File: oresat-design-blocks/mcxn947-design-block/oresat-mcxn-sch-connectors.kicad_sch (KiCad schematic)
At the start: 16 parts, among them J10 Conn_02x20_Odd_Even, J2 USB_C_Receptacle_USB2.0_14P, J9 Conn_02x20_Odd_Even, U1 MCXN947VKLT

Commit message: Updated BOM with MPNs and fixed one missing 0805 footprint error, rev'd board to v1.1
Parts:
- C1: MFR (none) -> Murata Electronics; MPN (none) -> GRM188R72A104KA35D
- J10, J9: MFR (none) -> Adam Tech; MPN (none) -> PH2-20-UA
- J2: MFR (none) -> GCT; MPN (none) -> USB4105-GF-A
- J7: value ~ -> OreSat Debug; MFR (none) -> TE; MPN (none) -> 2-1734592-0
- R1, R2: MFR (none) -> Stackpole Electronics Inc; MPN (none) -> RMCF0603FT5K11
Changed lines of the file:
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@@
 			)
 		)
-		(property "Description" "Resistor, small US symbol"
+		(property "Description" "5.11 kOhms ±1% 0.1W, 1/10W Chip Resistor 0603 (1608 Metric) Automotive AEC-Q200 Thick Film"
+			(at 306.07 90.17 0)
+			(effects
+				(font
+					(size 1.27 1.27)
+				)
+				(hide yes)
+			)
+		)
+		(property "MFR" "Stackpole Electronics Inc"
+			(at 306.07 90.17 0)
+			(effects
+				(font
+					(size 1.27 1.27)
+				)
+				(hide yes)
+			)
+		)
+		(property "MPN" "RMCF0603FT5K11"
 			(at 306.07 90.17 0)
 			(effects
@@
 			)
 		)
+		(property "MFR" "Adam Tech"
+			(at 100.33 177.8 0)
+			(effects
+				(font
+					(size 1.27 1.27)
+				)
+				(hide yes)
+			)
+		)
+		(property "MPN" "PH2-20-UA"
+			(at 100.33 177.8 0)
+			(effects
+				(font
+					(size 1.27 1.27)
+				)
+				(hide yes)
+			)
+		)
 		(pin "35"
 		)
@@
 			)
 		)
-		(property "Value" "~"
+		(property "Value" "OreSat Debug"
 			(at 367.03 71.12 0)
 			(effects
@@
 			)
 		)
-		(property "Datasheet" ""
+		(property "Datasheet" "https://www.te.com/usa-en/product-2-1734592-0.datasheet.pdf"
+			(at 367.03 71.12 0)
+			(effects
+				(font
+					(size 1.27 1.27)
+				)
+				(hide yes)
+			)
+		)
+		(property "Description" "20 Position FPC Connector Contacts, Bottom 0.020\" (0.50mm) Surface Mount, Right Angle"
+			(at 367.03 71.12 0)
+			(effects
+				(font
+					(size 1.27 1.27)
+				)
+				(hide yes)
+			)
+		)
+		(property "MFR" "TE"
 			(at 367.03 71.12 0)
 			(effects
@@
 			)
 		)
-		(property "Description" ""
+		(property "MPN" "2-1734592-0"
 			(at 367.03 71.12 0)
 			(effects
@@
 			)
 		)
-		(property "Description" "Resistor, small US symbol"
+		(property "Description" "5.11 kOhms ±1% 0.1W, 1/10W Chip Resistor 0603 (1608 Metric) Automotive AEC-Q200 Thick Film"
+			(at 312.42 90.17 0)
+			(effects
+				(font
+					(size 1.27 1.27)
+				)
+				(hide yes)
+			)
+		)
+		(property "MFR" "Stackpole Electronics Inc"
+			(at 312.42 90.17 0)
+			(effects
+				(font
+					(size 1.27 1.27)
+				)
+				(hide yes)
+			)
+		)
+		(property "MPN" "RMCF0603FT5K11"
 			(at 312.42 90.17 0)
 			(effects
@@
 			)
 		)
+		(property "MFR" "Adam Tech"
+			(at 110.49 82.55 0)
+			(effects
+				(font
+					(size 1.27 1.27)
+				)
+				(hide yes)
+			)
+		)
+		(property "MPN" "PH2-20-UA"
+			(at 110.49 82.55 0)
+			(effects
+				(font
+					(size 1.27 1.27)
+				)
+				(hide yes)
+			)
+		)
 		(pin "35"
 		)
@@
 			)
 		)
-		(property "Datasheet" "~"
+		(property "Datasheet" "https://search.murata.co.jp/Ceramy/image/img/A01X/G101/ENG/GRM188R72A104KA35-01.pdf"
 			(at 275.59 91.44 0)
 			(effects
@@
 			)
 		)
-		(property "Description" "Unpolarized capacitor, small symbol"
+		(property "Description" "0.1 µF ±10% 100V Ceramic Capacitor X7R 0603 (1608 Metric)"
+			(at 275.59 91.44 0)
+			(effects
+				(font
+					(size 1.27 1.27)
+				)
+				(hide yes)
+			)
+		)
+		(property "MFR" "Murata Electronics"
+			(at 275.59 91.44 0)
+			(effects
+				(font
+					(size 1.27 1.27)
+				)
+				(hide yes)
+			)
+		)
+		(property "MPN" "GRM188R72A104KA35D"
 			(at 275.59 91.44 0)
 			(effects
@@
 			)
 		)
-		(property "Datasheet" "https://www.usb.org/sites/default/files/documents/usb_type-c.zip"
+		(property "Datasheet" "https://gct.co/files/specs/usb4105-spec.pdf"
 			(at 287.02 63.5 0)
 			(effects
@@
 			)
 		)
-		(property "Description" "USB 2.0-only 14P Type-C Receptacle connector"
+		(property "Description" "USB-C (USB TYPE-C) USB 2.0 Receptacle Connector 24 (16+8 Dummy) Position Surface Mount, Right Angle; Through Hole"
+			(at 283.21 63.5 0)
+			(effects
+				(font
+					(size 1.27 1.27)
+				)
+				(hide yes)
+			)
+		)
+		(property "MFR" "GCT"
+			(at 283.21 63.5 0)
+			(effects
+				(font
+					(size 1.27 1.27)
+				)
+				(hide yes)
+			)
+		)
+		(property "MPN" "USB4105-GF-A"
 			(at 283.21 63.5 0)
 			(effects

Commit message: Cleanup of page names and put all power/connectors and signals on the same page facing the same way
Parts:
- removed J10, J9: Conn_02x20_Odd_Even, Connector_PinHeader_2.54mm:PinHeader_2x20_P2.54mm_Vertical, symbol Connector_Generic:Conn_02x20_Odd_Even
- removed U1: MCXN947VKLT, oresat-ics:MCXN947KVLT-QFP50P1600X1600X160-101N, symbol oresat-ics:MCXN947VKLT
- added C10: 6.8u, oresat-passives:0603-C-NOSILK, symbol Device:C_Small
- added C11, C7: 4.7u, oresat-passives:0603-C-NOSILK, symbol Device:C_Small
- added C12, C13, C14, C15, C16, C2, C20, C3, C8, C9: 100n, oresat-passives:0603-C-NOSILK, symbol Device:C_Small
- added C17, C4: 1u, oresat-passives:0603-C-NOSILK, symbol Device:C_Small
- added C18: 22u, oresat-passives:0805-C-NOSILK, symbol Device:C
- added C5: 10u, oresat-passives:0603-C-NOSILK, symbol Device:C
- added C6: 2.2u, oresat-passives:0603-C-NOSILK, symbol Device:C_Small
- added D1: BAT54CW, Package_TO_SOT_SMD:SOT-323_SC-70, symbol Diode:BAT54CW
- added D6: GREEN, LED_SMD:LED_0603_1608Metric, symbol Device:LED_Small_Filled
- added FB1: 120 ohm, oresat-passives:0805-B-NOSILK, symbol Device:FerriteBead_Small
- added J1: BKUP-BATT, Connector_PinHeader_2.54mm:PinHeader_1x02_P2.54mm_Vertical, symbol Connector_Generic:Conn_01x02
- added L1: 1.5u, Inductor_SMD:L_0805_2012Metric, symbol Device:L_Small
- added L2: 6.8u, oresat-passives:L_ECS-MPI4040, symbol oresat-passives:L_BIG
- added R10, R11, R12: 10k, oresat-passives:0603-C-NOSILK, symbol oresat-passives:R-US
- added R3: 10k, oresat-passives:0603-C-NOSILK, symbol Device:R_Small_US
- added TP1, TP2, TP3, TP33, TP34, TP4: Test-Point, oresat-misc:TestPoint-0.75mm-th, symbol oresat-misc:Test-Point-0.75mm-th
- added U1: MCXN947VKLT, oresat-ics:MCXN947KVLT-QFP50P1600X1600X160-101N, symbol oresat-ics:MCXN947VKLT
- added U3: TPS62111RSA, Package_DFN_QFN:Texas_RSA_VQFN-16-1EP_4x4mm_P0.65mm_EP2.7x2.7mm, symbol oresat-ics:TPS6211X
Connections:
- net +3.3V: now also C12.1, C13.1, C14.1, C15.1, C16.1, C18.1, C7.1, C8.1, C9.1, D1.2, FB1.1, L2.2, R10.2, R3.2, TP34.1, U1.34 (VDD_P4), U1.44 (VDD_USB), U1.54 (VDD_DCDC/VDD_LDO_SYS), U1.59 (VDD_P3_1), U1.66 (VDD_P3_2), U1.73 (VDD_P3_3), U1.83 (VDD_1), U1.96 (VDD_2), U3.10 (FB)
- net GND: now also C10.2, C11.2, C12.2, C13.2, C14.2, C15.2, C16.2, C17.2, C18.2, C2.2, C20.2, C3.2, C4.2, C5.2, C6.2, C7.2, C8.2, C9.2, D6.1 (K), J1.2 (Pin_2), R11.1, U1.101 (EP), U1.32 (VREFL), U1.33 (VSS_P4), U1.52 (VSS_DCDC), U3.1 (GND), U3.11 (GND), U3.12 (GND), U3.16 (GND), U3.17 (GND), U3.6 (LBO), U3.7 (LBI), U3.9 (GND)
- net RESET: now also C20.1, R3.1, TP4.1, U1.9 (RESET_B)
- net USB_D+: now also U1.46 (USB0_DP)
- net USB_D-: now also U1.45 (USB0_DM)
- net VBUS: now also C17.1, C5.1, R12.2, U3.2 (VIN), U3.3 (VIN), U3.4 (EN), U3.8 (VINA)
- new net: D1.3, TP3.1, U1.47 (VDD_BAT)
- new net: L2.1, U3.14 (SW), U3.15 (SW)
- new net: R11.2, R12.1, TP33.1, U3.5 (SYNC)
- new net: C6.1, U1.55 (VDD_SYS)
- new net: C4.1, FB1.2, TP1.1, U1.30 (VDD_ANA), U1.31 (VREFH)
- new net: D6.2 (A), R10.1
- new net: D1.1, J1.1 (Pin_1)
- new net: L1.2, U1.53 (DCDC_LX)
- new net VDD: C10.1, C11.1, C2.1, C3.1, L1.1, TP2.1, U1.12 (VDD_CORE_1), U1.13 (VDD_LDO_CORE/VDD/VDD_P2), U1.58 (VDD_CORE_2)
- no-connect marks 4 -> 5
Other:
- note added: "0805"
- note added: "Design notes on table 3 of data sheet"
- note added: "Note: Disable LDO_CORE in software for more power savings"
- note added: "OUT"
- note added: "P0/P1"
- note added: "See also USB0_VBUS_DET"
- note added: "VDD_CORE"
- note removed: "15 unused pins"
- note removed: "16 unused pins"
- note removed: "8 unused pins"
- note removed: "USB0_VUS_DET"
- note removed: "free available pins"
- moved on the sheet: C1, J2, R1, R2, TP13, TP14, TP15, TP16

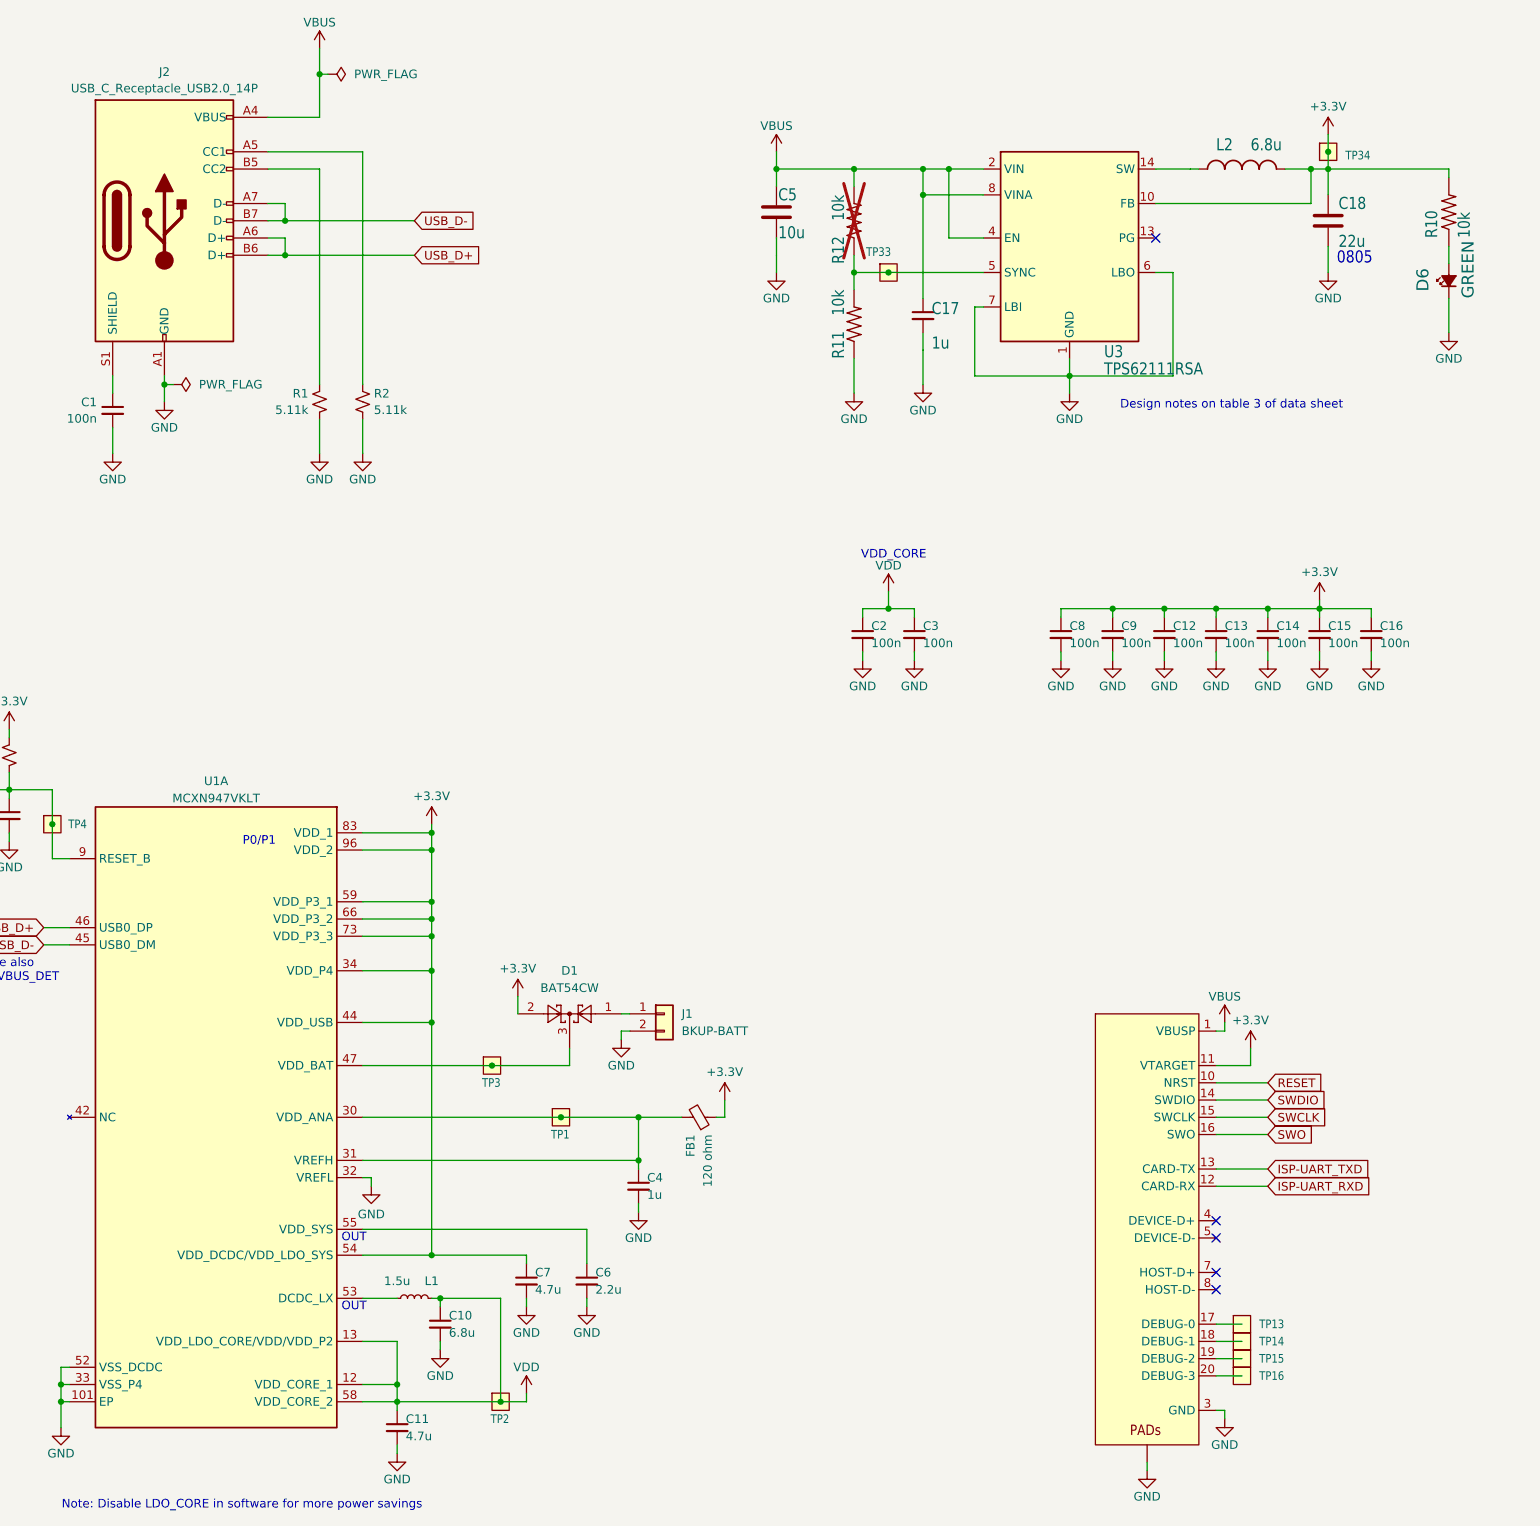
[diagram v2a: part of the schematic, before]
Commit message: Fixed MCXN center pad paste, re-arranged MCXN power pins, and fixed breakout board to hopefully not short.
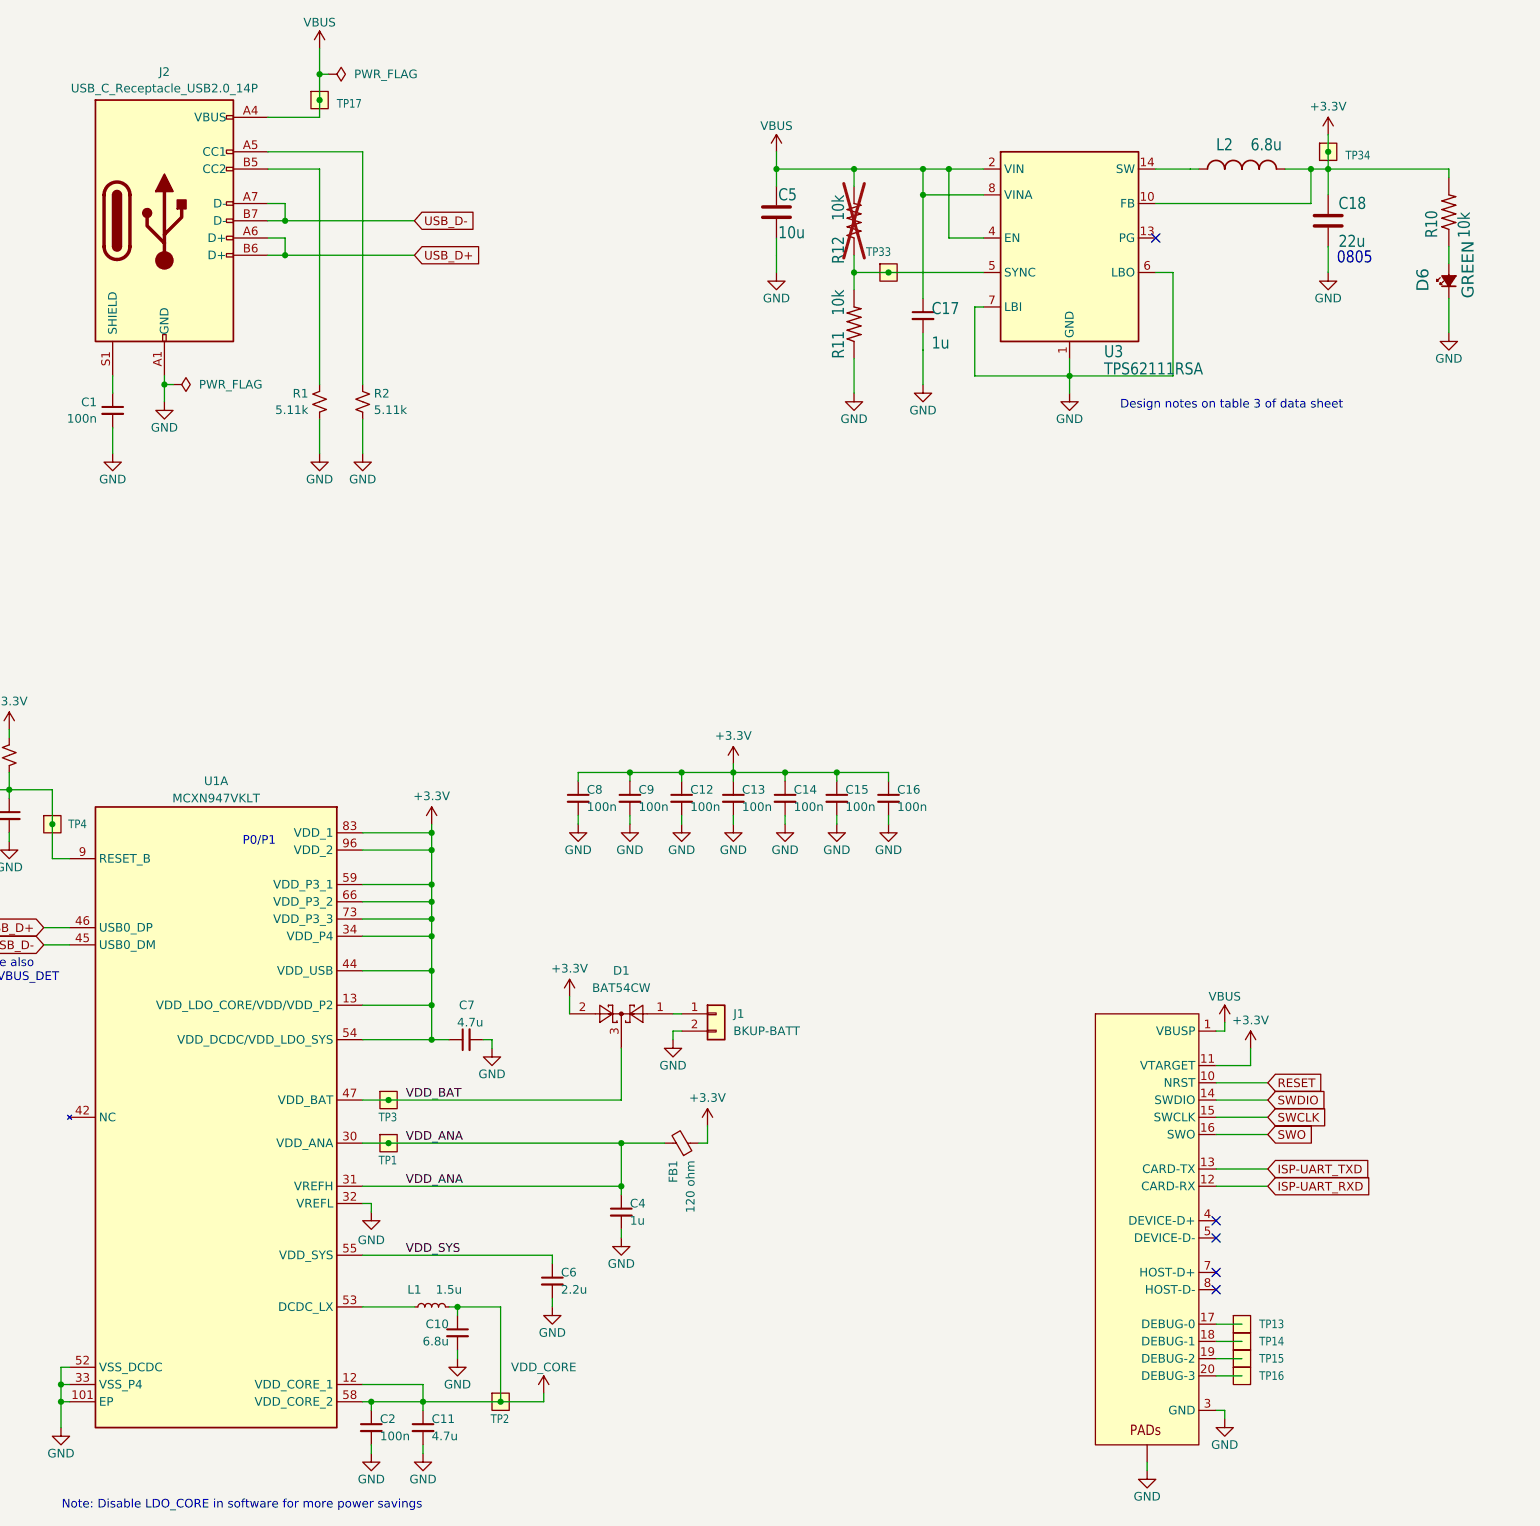
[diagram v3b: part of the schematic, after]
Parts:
- removed C3: 100n, oresat-passives:0603-C-NOSILK, symbol Device:C_Small
- added TP17: Test-Point, oresat-misc:TestPoint-0.75mm-th, symbol oresat-misc:Test-Point-0.75mm-th
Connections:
- net +3.3V: now also U1.13 (VDD_LDO_CORE/VDD/VDD_P2)
- net VBUS: now also TP17.1
- net VDD_BAT: now reaches D1.3, TP3.1, U1.47 (VDD_BAT)
- net VDD_SYS: now reaches C6.1, U1.55 (VDD_SYS)
- net VDD_ANA: now reaches C4.1, FB1.2, TP1.1, U1.30 (VDD_ANA), U1.31 (VREFH)
- net VDD renamed VDD_CORE
- net VDD_CORE: no longer U1.13 (VDD_LDO_CORE/VDD/VDD_P2)
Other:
- note removed: "OUT"
- note removed: "VDD_CORE"
- moved on the sheet: C10, C11, C12, C13, C14, C15, C16, C2, C4, C6, C7, C8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
